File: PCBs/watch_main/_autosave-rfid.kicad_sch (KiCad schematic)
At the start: 45 parts, among them IC1701 TLV9004SIRTER, IC1702 MAX9027EBT+T, Q1701 DMN21D2UFB-7B, Q1702 DMP21D5UFB4-7B, Q1703 DMN21D2UFB-7B, Q1704 DMN21D2UFB-7B

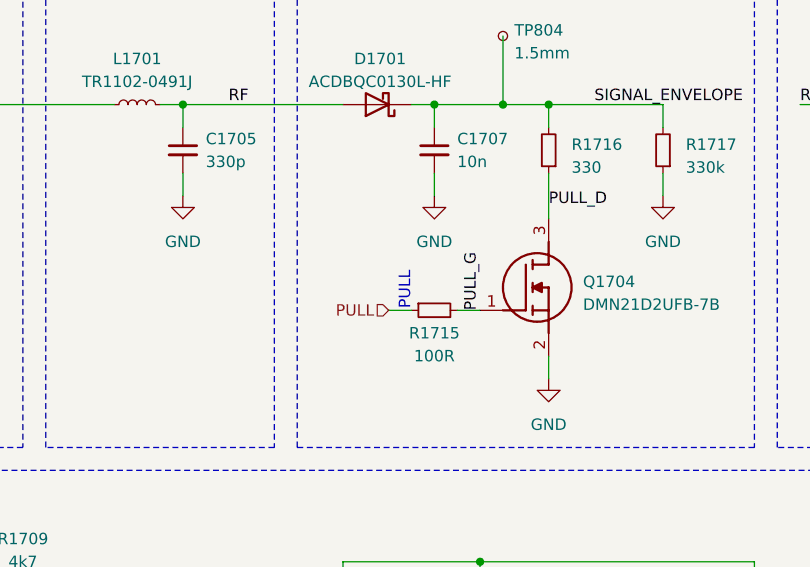
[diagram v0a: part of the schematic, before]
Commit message: 287 Connections unrouted
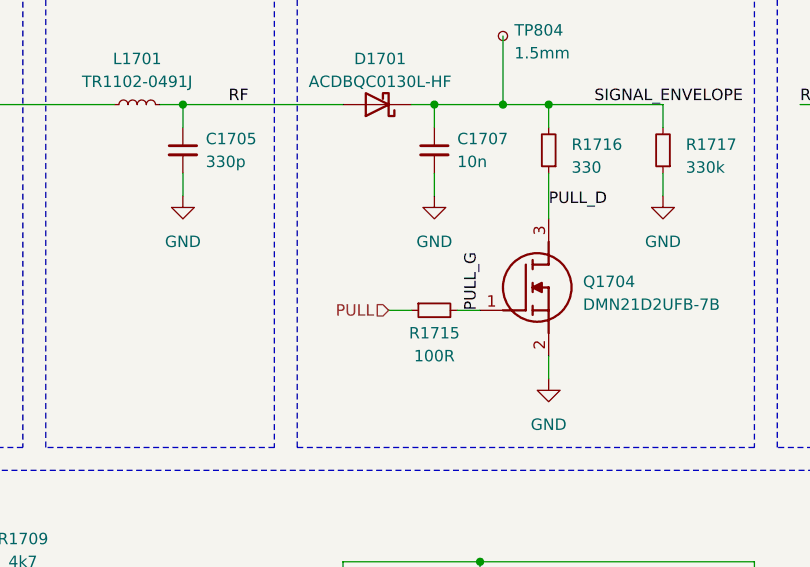
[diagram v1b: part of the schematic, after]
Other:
- note removed: "PULL"
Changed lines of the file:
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@@
-    (effects (font (size 1.27 1.27)) (justify left bottom))
-  )
-  (text "PULL" (at 144.78 76.2 90)
     (effects (font (size 1.27 1.27)) (justify left bottom))
   )
